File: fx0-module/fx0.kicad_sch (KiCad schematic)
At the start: 30 parts, among them J1 Line IN, J2 CV IN, J3 Line OUT, J4 CV OUT, U1 SeeeduinoXIAO, U2 Pico, U3 ProMicro

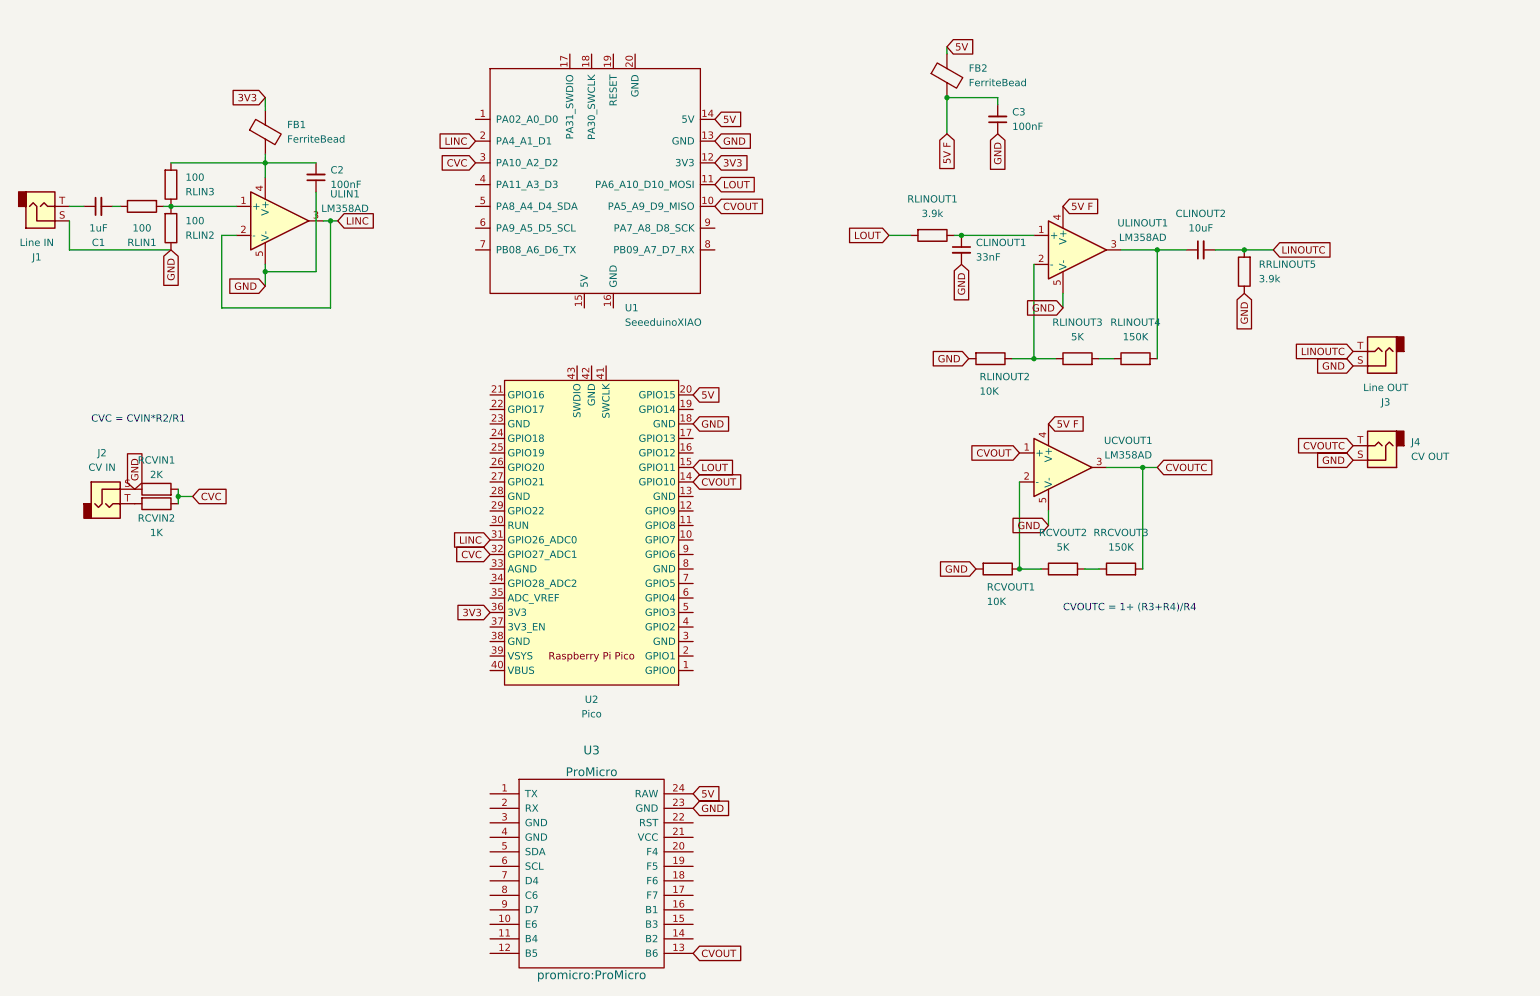
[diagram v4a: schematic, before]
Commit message: Redraw pcb with proper op amp legs and no seeduino
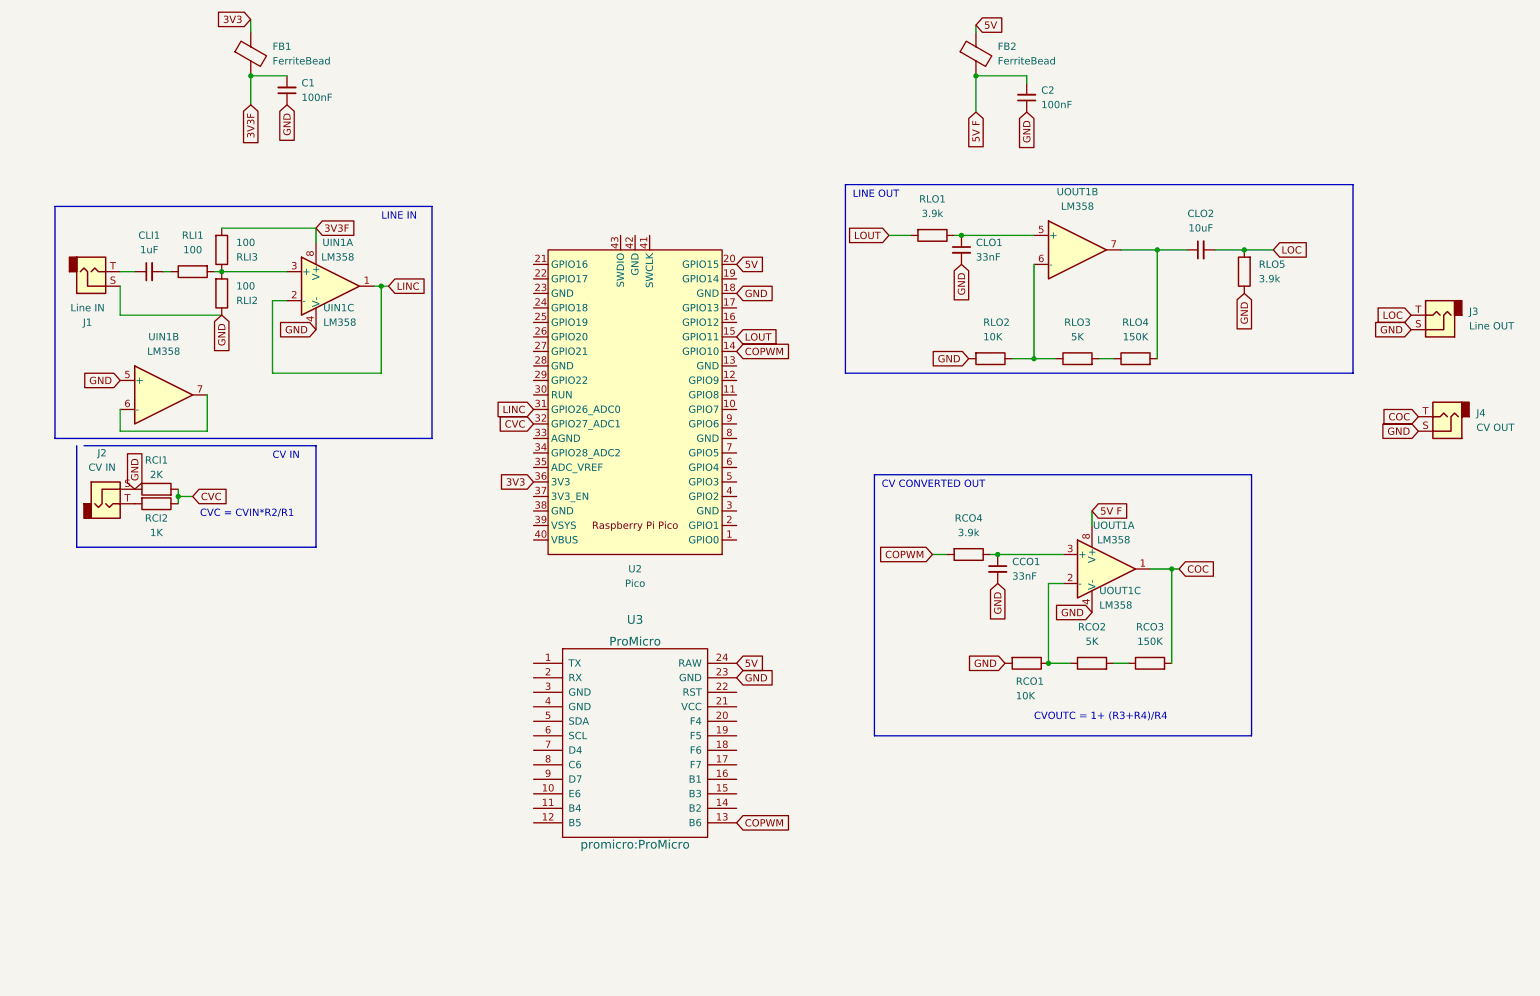
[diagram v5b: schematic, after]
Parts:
- removed C2: 100nF, Capacitor_SMD:C_0805_2012Metric_Pad1.18x1.45mm_HandSolder, symbol Device:C_Small
- removed RCVOUT1: 10K, Resistor_SMD:R_0805_2012Metric_Pad1.20x1.40mm_HandSolder, symbol Device:R
- removed RCVOUT2: 5K, Resistor_SMD:R_0805_2012Metric_Pad1.20x1.40mm_HandSolder, symbol Device:R
- removed RRCVOUT3: 150K, Resistor_SMD:R_0805_2012Metric_Pad1.20x1.40mm_HandSolder, symbol Device:R
- removed U1: SeeeduinoXIAO, Seeeduino XIAO KICAD:Seeeduino XIAO-MOUDLE14P-2.54-21X17.8MM, symbol Seeeduino XIAO:SeeeduinoXIAO
- removed UCVOUT1, ULIN1, ULINOUT1: LM358AD, Package_SO:SOP-8_3.9x4.9mm_P1.27mm, symbol pspice:OPAMP
- added C1: 100nF, Capacitor_SMD:C_0805_2012Metric_Pad1.18x1.45mm_HandSolder, symbol Device:C_Small
- added CCO1: 33nF, Capacitor_SMD:C_0805_2012Metric_Pad1.18x1.45mm_HandSolder, symbol Device:C_Small
- added RCO1: 10K, Resistor_SMD:R_0805_2012Metric_Pad1.20x1.40mm_HandSolder, symbol Device:R
- added RCO2: 5K, Resistor_SMD:R_0805_2012Metric_Pad1.20x1.40mm_HandSolder, symbol Device:R
- added RCO3: 150K, Resistor_SMD:R_0805_2012Metric_Pad1.20x1.40mm_HandSolder, symbol Device:R
- added RCO4: 3.9k, Resistor_SMD:R_0805_2012Metric_Pad1.20x1.40mm_HandSolder, symbol Device:R
- added UIN1, UOUT1: LM358, Package_SO:SOP-8_3.9x4.9mm_P1.27mm, symbol Amplifier_Operational:LM358
- renumbered C3 to C2, C1 to CLI1, CLINOUT1 to CLO1, CLINOUT2 to CLO2, RCVIN1 to RCI1, RCVIN2 to RCI2, RLIN1 to RLI1, RLIN2 to RLI2, RLIN3 to RLI3, RLINOUT1 to RLO1, RLINOUT2 to RLO2, RLINOUT3 to RLO3, RLINOUT4 to RLO4, RRLINOUT5 to RLO5
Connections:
- net 5V F: now also UOUT1.8 (V+)
- net GND: now also C1.1, CCO1.2, RCO1.2, UIN1.4 (V-), UIN1.5 (+), UOUT1.4 (V-)
- net LINC: now also UIN1.1, UIN1.2 (-)
- net at CLO2.1, RLO4.2: now also UOUT1.7
- net at CLO1.1, RLO1.1: now also UOUT1.5 (+)
- net at RLO2.1, RLO3.1: now also UOUT1.6 (-)
- net at RLI1.2, RLI2.2, RLI3.1: now also UIN1.3 (+)
- net 3V3F: now reaches FB1.2, RLI3.2
- net 3V3F: now also C1.2, UIN1.8 (V+)
- net CVOUT renamed COPWM
- net COPWM: now also RCO4.2
- net CVOUTC renamed COC
- net COC: now also RCO3.2, UOUT1.1
- net LINOUTC renamed LOC
- new net: CCO1.1, RCO4.1, UOUT1.3 (+)
- new net: RCO1.1, RCO2.1, UOUT1.2 (-)
- new net: UIN1.6 (-), UIN1.7
- new net: RCO2.2, RCO3.1
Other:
- note added: "CV CONVERTED OUT"
- note added: "CV IN"
- note added: "LINE IN"
- note added: "LINE OUT"
- moved on the sheet: C2, CLI1, FB1, FB2, J1, J3, J4, RLI1, RLI2, RLI3, U2, U3

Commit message: Change value for rc filter
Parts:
- RCO4: value 3.9k -> (none)
- RLI1: value 100 -> 24k
- RLI2, RLI3: value 100 -> 47k
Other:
- note added: "45khz"
- note added: "48hz cutoff"
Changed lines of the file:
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@@
     (stroke (width 0) (type default) (color 0 0 0 0))
+  )
+  (text "45khz\n" (at 171.45 109.22 180)
+    (effects (font (size 1.27 1.27)) (justify right bottom))
   )
   (text "CVC = CVIN*R2/R1" (at 45.72 104.14 0)
@@
     (effects (font (size 1.27 1.27)) (justify left bottom))
   )
+  (text "48hz\ncutoff" (at 182.88 116.84 180)
+    (effects (font (size 1.27 1.27)) (justify right bottom))
+  )
   (global_label "GND" (shape input) (at 139.7 132.08 0) (fields_autoplaced)
     (effects (font (size 1.27 1.27)) (justify left))
@@
     (in_bom yes) (on_board yes) (fields_autoplaced)
     (property "Reference" "RCO4" (id 0) (at 180.34 104.14 90))
-    (property "Value" "3.9k" (id 1) (at 180.34 106.68 90))
+    (property "Value" "" (id 1) (at 180.34 106.68 90))
     (property "Footprint" "Resistor_SMD:R_0805_2012Metric_Pad1.20x1.40mm_HandSolder" (id 2) (at 180.34 108.712 90)
       (effects (font (size 1.27 1.27)) hide)
@@
       (effects (font (size 1.27 1.27)) (justify left))
     )
-    (property "Value" "100" (id 1) (at 52.07 55.8801 0)
+    (property "Value" "47k" (id 1) (at 52.07 55.8801 0)
       (effects (font (size 1.27 1.27)) (justify left))
     )
@@
       (effects (font (size 1.27 1.27)) (justify left))
     )
-    (property "Value" "100" (id 1) (at 52.07 63.5001 0)
+    (property "Value" "47k" (id 1) (at 52.07 63.5001 0)
       (effects (font (size 1.27 1.27)) (justify left))
     )
@@
     (in_bom yes) (on_board yes) (fields_autoplaced)
     (property "Reference" "RLI1" (id 0) (at 44.45 54.61 90))
-    (property "Value" "100" (id 1) (at 44.45 57.15 90))
+    (property "Value" "24k" (id 1) (at 44.45 57.15 90))
     (property "Footprint" "Resistor_SMD:R_0805_2012Metric_Pad1.20x1.40mm_HandSolder" (id 2) (at 44.45 59.182 90)
       (effects (font (size 1.27 1.27)) hide)
@@
     )
     (path "/130ae569-e2dc-4995-bf7a-e97b18b6bb7c"
-      (reference "RCO4") (unit 1) (value "3.9k") (footprint "Resistor_SMD:R_0805_2012Metric_Pad1.20x1.40mm_HandSolder")
+      (reference "RCO4") (unit 1) (value "100k") (footprint "Resistor_SMD:R_0805_2012Metric_Pad1.20x1.40mm_HandSolder")
     )
     (path "/9f8391bb-e1c3-47de-acf1-ec8ef46448c9"
-      (reference "RLI1") (unit 1) (value "100") (footprint "Resistor_SMD:R_0805_2012Metric_Pad1.20x1.40mm_HandSolder")
+      (reference "RLI1") (unit 1) (value "24k") (footprint "Resistor_SMD:R_0805_2012Metric_Pad1.20x1.40mm_HandSolder")
     )
     (path "/9b0faa99-ce75-4972-80b5-6486a909d46b"
-      (reference "RLI2") (unit 1) (value "100") (footprint "Resistor_SMD:R_0805_2012Metric_Pad1.20x1.40mm_HandSolder")
+      (reference "RLI2") (unit 1) (value "47k") (footprint "Resistor_SMD:R_0805_2012Metric_Pad1.20x1.40mm_HandSolder")
     )
     (path "/7a9c1370-8319-4c6b-ab8c-15e7acd67613"
-      (reference "RLI3") (unit 1) (value "100") (footprint "Resistor_SMD:R_0805_2012Metric_Pad1.20x1.40mm_HandSolder")
+      (reference "RLI3") (unit 1) (value "47k") (footprint "Resistor_SMD:R_0805_2012Metric_Pad1.20x1.40mm_HandSolder")
     )
     (path "/ee96104d-208a-40dd-948b-cf2cdf6fe860"
